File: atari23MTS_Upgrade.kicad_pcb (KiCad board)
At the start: 2 copper layers, 98 x 119.5 mm, 83 parts, among them J1 Conn_01x02, J2 Conn_01x02, J3 Conn_01x02, J4 Conn_01x02, J5 Conn_01x02, J6 Conn_01x02, J7 Conn_01x02, J8 Conn_01x02, J9 Micro_SD_Card_Det, P1 CONN_01X01, P2 CONN_01X01, P3 CONN_01X01, P4 CONN_01X01, P5 CONN_01X01, P6 CONN_01X01, P7 CONN_01X01, P8 CONN_01X01, SW1 SW_Push, U1 NCP1117ST33T3G, U10 74LVC2G32, U11 74LVC2G08, U12 74LVC2G74, U13 STM32F407VETx, U2 TXB0108-PW, U3 TXB0108-PW, U4 TXB0108-PW, U5 TXB0108-PW, U6 TXB0108-PW, U7 ISSI61WV5128BL, U8 ISSI61WV5128BL, U9 74HCT04

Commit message: Cosmetic issues
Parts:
- moved C1 7.62 mm to (123.2, 94.0)
- moved C11 7.62 mm to (121.2, 104.4)
- moved C2 7.62 mm to (103.6, 94.0)
- moved C3 7.62 mm to (104.9, 101.3)
- moved C6 7.62 mm to (139.7, 88.9)
- moved CART1 7.62 mm to (148.1, 133.9)
- moved CART2 7.62 mm to (166.4, 113.0)
- moved D1 7.62 mm to (113.5, 87.9)
- moved D2 7.62 mm to (113.5, 104.4)
- moved D4 7.62 mm to (147.3, 91.4)
- moved DUOCART 7.62 mm to (110.5, 76.2)
- moved ECI1 7.62 mm to (108.0, 147.3)
- moved ECI2 7.62 mm to (127.0, 113.0)
- moved EXTPWR1 7.62 mm to (108.0, 55.9)
- moved Kicad 7.62 mm to (155.0, 81.6)
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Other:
- board text added: "+12V"
- board text added: "+5V"
- board text added: "GND"

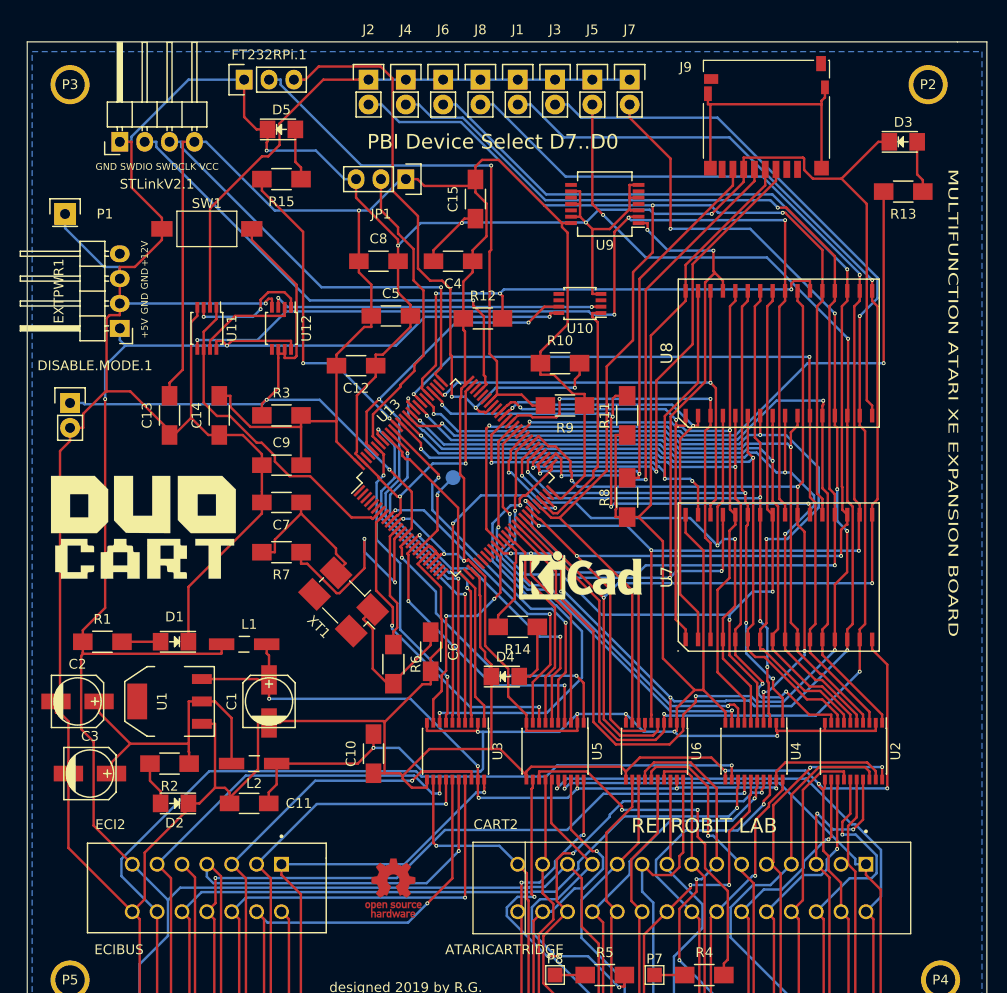
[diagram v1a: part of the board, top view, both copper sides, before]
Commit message: Modified CPU STM32F407VG
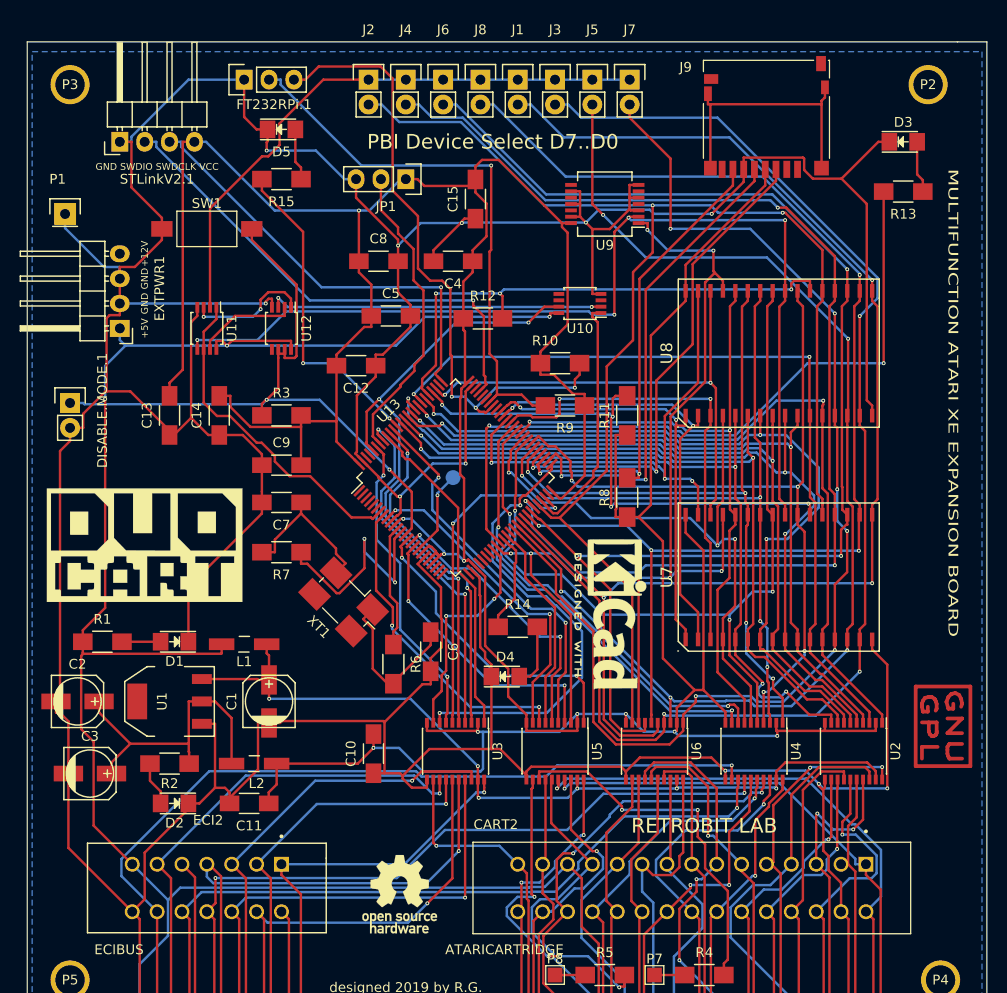
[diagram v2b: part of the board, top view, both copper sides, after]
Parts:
- removed ATARILOGO: LOGO, RetroBitLab:atari_fuji_SilkScreen_21.2x25-RevBack
- removed the DUOCART at (110.5, 76.2)
- removed Kicad: KiCad-Logo_5mm_SilkScreen, Symbol:KiCad-Logo_5mm_SilkScreen
- removed OSHW: OSHW-Logo_5.7x6mm_Copper, Symbol:OSHW-Logo_5.7x6mm_Copper
- added DUOCART: LOGO, RetroBitLab:DUOCart_20x11, F.Cu at (110.5, 78.0)
- added G***: LOGO, RetroBitLab:atari_fuji_SilkScreen_21.2x25-RevBack, B.Cu at (142.2, 55.9)
- added GPL: Symbol_GNU-GPL_CopperTop_Small, Symbol:Symbol_GNU-GPL_CopperTop_Small, F.Cu at (191.8, 96.5)
- added KICAD: KiCad-Logo2_6mm_SilkScreen, Symbol:KiCad-Logo2_6mm_SilkScreen, F.Cu at (158.8, 85.1)
- added REF**: OSHW-Logo_7.5x8mm_SilkScreen, Symbol:OSHW-Logo_7.5x8mm_SilkScreen, F.Cu at (136.5, 113.7)
- U13: value STM32F407VETx -> STM32F407VGTx
- moved G*** 2.84 mm to (142.2, 81.3)

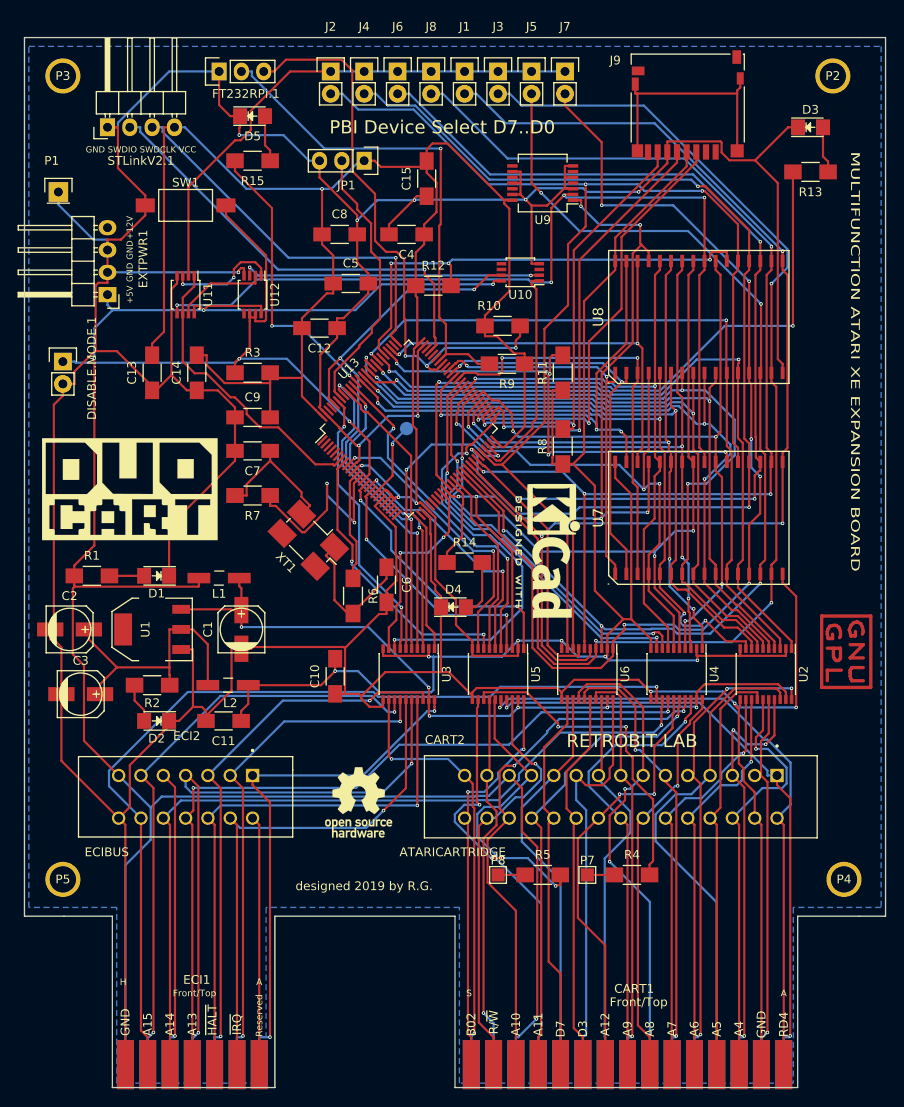
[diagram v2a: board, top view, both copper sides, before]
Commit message: added fill zone top layer
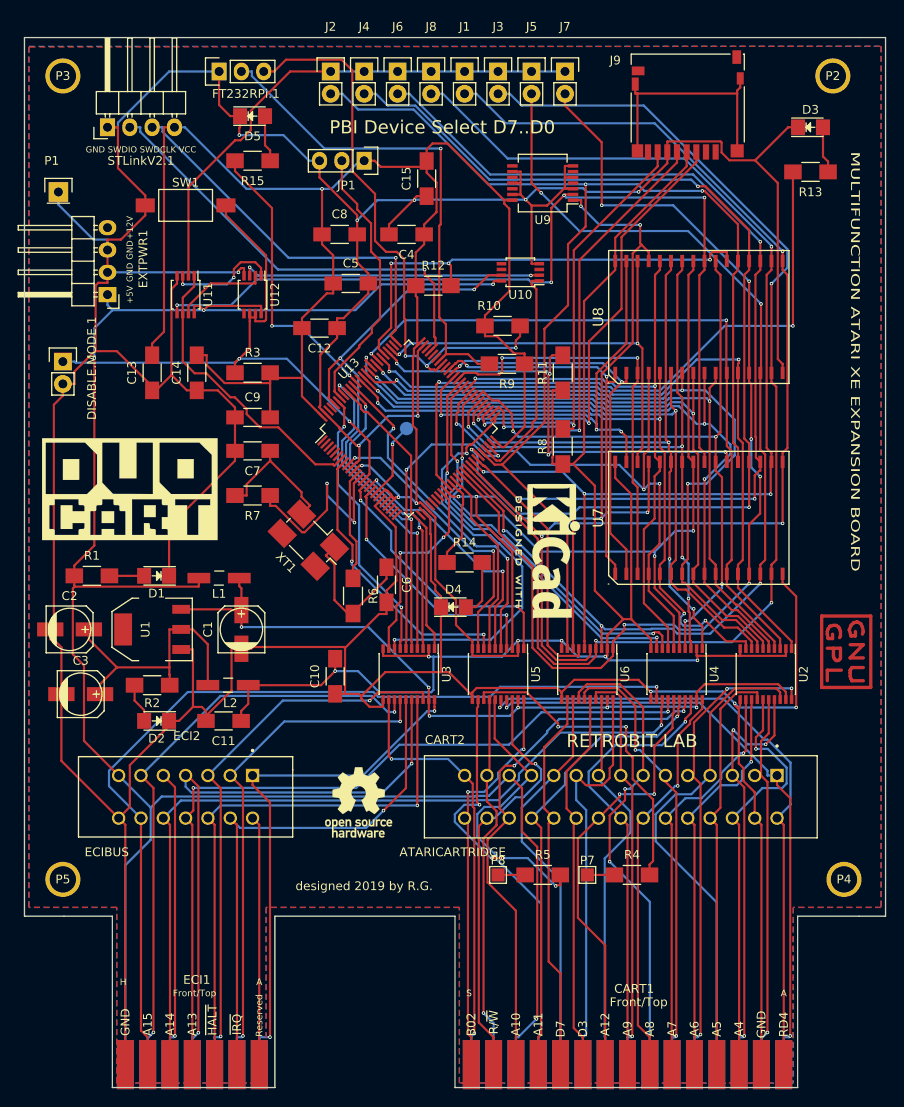
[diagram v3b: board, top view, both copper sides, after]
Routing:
- added copper zone on F.Cu, net GND
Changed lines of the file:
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@@
 (kicad_pcb (version 4) (host pcbnew 4.0.2+dfsg1-stable)
   (general
-    (links 0)
+    (links 357)
     (no_connects 0)
     (area 71.285716 17.15 198.15 162.820001)
@@
       )
     )
+  )
+  (zone (net 1) (net_name GND) (layer F.Cu) (hatch edge 0.508)
+    (connect_pads (clearance 0.508))
+    (min_thickness 0.254)
+    (fill yes (arc_segments 16) (thermal_gap 0.508) (thermal_bridge_width 0.508))
+    (polygon
+      (pts
+        (xy 99.1 27.7) (xy 196 27.6) (xy 196 125.6) (xy 186 125.6) (xy 185.9 145.6)
+        (xy 148 145.6) (xy 148 125.6) (xy 126 125.6) (xy 126 145.6) (xy 109 145.6)
+        (xy 109 125.6) (xy 99 125.6) (xy 99 27.7)
+      )
+    )

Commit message: Modified for dual processors board
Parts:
- removed DUOCART: LOGO, RetroBitLab:DUOCart_20x11
- removed G***: LOGO, RetroBitLab:atari_fuji_SilkScreen_21.2x25-RevBack
- removed G***: LOGO, RetroBitLab:atari_800_XL_BW_25x25
- removed GPL: Symbol_GNU-GPL_CopperTop_Small, Symbol:Symbol_GNU-GPL_CopperTop_Small
- removed J1, J2, J3, J4, J5, J6, J7, J8: Conn_01x02, Pin_Headers:Pin_Header_Straight_1x02
- removed KICAD: KiCad-Logo2_6mm_SilkScreen, Symbol:KiCad-Logo2_6mm_SilkScreen
- removed REF**: OSHW-Logo_7.5x8mm_SilkScreen, Symbol:OSHW-Logo_7.5x8mm_SilkScreen
- added C16: 20p, Capacitors_SMD:C_1206_HandSoldering, F.Cu at (390.3, 193.1)
- added C17: 20p, Capacitors_SMD:C_1206_HandSoldering, F.Cu at (385.0, 199.8)
- added C18: 100n, Capacitors_SMD:C_1206_HandSoldering, F.Cu at (405.9, 179.7)
- added C19: 100n, Capacitors_SMD:C_1206_HandSoldering, F.Cu at (397.4, 193.1)
- added C20: 100n, Capacitors_SMD:C_1206_HandSoldering, F.Cu at (383.3, 185.8)
- added C21: 100n, Capacitors_SMD:C_1206_HandSoldering, F.Cu at (392.1, 199.8)
- added C22: 100n, Capacitors_SMD:C_1206_HandSoldering, F.Cu at (404.4, 193.1)
- added C23: 100n, Capacitors_SMD:C_1206_HandSoldering, F.Cu at (411.5, 186.4)
- added C24: 100n, Capacitors_SMD:C_1206_HandSoldering, F.Cu at (399.1, 199.8)
- added DISABLE.MODE.2: CONN_01X02, Pin_Headers:Pin_Header_Straight_1x02, F.Cu at (348.2, 136.4)
- added JP2: CONN_01X03, Pin_Headers:Pin_Header_Straight_1x03, F.Cu at (336.8, 136.4)
- added P10: CONN_01X02, Pin_Headers:Pin_Header_Straight_1x02, F.Cu at (342.8, 193.2)
- added P11: CONN_01X02, Pin_Headers:Pin_Header_Straight_1x02, F.Cu at (329.8, 197.2)
- added P12: CONN_01X02, Pin_Headers:Pin_Header_Straight_1x02, F.Cu at (319.6, 207.9)
- added P13: CONN_01X02, Pin_Headers:Pin_Header_Straight_1x02, F.Cu at (353.0, 182.5)
- added P14: CONN_01X02, Pin_Headers:Pin_Header_Straight_1x02, F.Cu at (340.0, 204.0)
- added P9: CONN_01X02, Pin_Headers:Pin_Header_Straight_1x02, F.Cu at (319.6, 197.2)
- added R16: 220, Resistors_SMD:R_1206_HandSoldering, F.Cu at (391.8, 179.7)
- added STLinkV2.2: CONN_01X04, Pin_Headers:Pin_Header_Angled_1x04, F.Cu at (310.6, 136.4)
- added SW2: SW_Push, RetroBitLab:SW_SPST_FSMSM_3D, F.Cu at (341.0, 147.2)
- added U14: STM32F407VGTx, Housings_QFP:TQFP-100_14x14mm_Pitch0.5mm, F.Cu at (370.8, 186.8)
- added XT2: 8Mhz, RetroBitLab:Crystal_HC49-4H_Vertical_3D, F.Cu at (365.7, 201.9)
- D5: value LED.AMBER -> LED.GREEN
- P6: moved to F.Cu
- P7, P8: value CONN_01X01 -> CONN_01X02; footprint TestPoint:TestPoint_Pad_1.5x1.5mm -> Pin_Headers:Pin_Header_Straight_1x02
- R10: value 10k -> 0
- R11, R3: value 10K -> 220
- R13, R2: value 220 -> 10K
- R14, R15: value 220 -> 0
- R4: value 0 -> 10K
- R6: value 0 -> 220
- R7: value 220 -> 47k
- R8: value 47k -> 220
- R9: value 10k -> 220
- U13: footprint Housings_QFP:LQFP-100_14x14mm_Pitch0.5mm -> Housings_QFP:TQFP-100_14x14mm_Pitch0.5mm
- XT1: footprint Crystal:Crystal_SMD_0603-4Pin_6.0x3.5mm_HandSoldering -> RetroBitLab:Crystal_HC49-4H_Vertical_3D
- moved C5 353.1 mm to (479.8, 133.6)
- moved C4 350.0 mm to (479.8, 140.3), turned to 0 degrees
- moved U6 318.6 mm to (476.8, 151.3), turned to 0 degrees
- moved U5 318.3 mm to (466.4, 151.3), turned to 0 degrees
- moved R15 315.6 mm to (404.4, 186.4), turned to 0 degrees
- moved C13 310.5 mm to (414.2, 140.3), turned to 0 degrees
- moved U3 307.7 mm to (445.5, 151.3), turned to 0 degrees
- moved R7 303.1 mm to (421.2, 140.3), turned to 0 degrees
- moved U8 301.2 mm to (465.8, 138.0)
- moved C7 298.9 mm to (414.2, 147.0), turned to 0 degrees
- moved D5 296.7 mm to (384.0, 179.4)
- moved C11 294.5 mm to (414.2, 133.6)
- moved C15 291.5 mm to (421.2, 133.6), turned to 0 degrees
- moved C9 291.3 mm to (407.1, 140.3)
- moved C14 289.5 mm to (392.2, 157.8), turned to 0 degrees
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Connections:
- net BOOT0 renamed BOOT0_CART
- net SWDCLK renamed SWDCLK_CART
- net SWDIO renamed SWDIO_CART
- DISABLE.MODE.1 pad 1: nRESET -> nRESET_CART
- FT232RPi.1 pad 2: UART_RX_TTL -> UART_RX
- FT232RPi.1 pad 3: UART_TX_TTL -> UART_TX
- P7 pad 1: Net-(P7-Pad1) -> mD0
- P8 pad 1: Net-(P8-Pad1) -> mD1
- R10 pad 1: VCC3V3 -> Net-(R10-Pad1)
- R10 pad 2: UART_TX_TTL -> Net-(C16-Pad1)
- R11 pad 1: VCC3V3 -> Net-(R11-Pad1)
- R11 pad 2: ~mCHIP0 -> Net-(C17-Pad1)
- R12 pad 1: VCC3V3 -> GND
- R12 pad 2: ~mCHIP1 -> UART_TX
- R13 pad 1: Net-(D3-Pad2) -> GND
- R13 pad 2: LEDGRN -> UART_RX
- R14 pad 1: Net-(D4-Pad2) -> mB6
- R14 pad 2: LEDRED -> GND
- R15 pad 1: Net-(D5-Pad2) -> mB7
- R15 pad 2: LEDAMBER -> GND
- R2 pad 1: Net-(C2-Pad1) -> nRESET_CART
- R2 pad 2: Net-(D2-Pad2) -> VCC3V3
- R3 pad 1: nRESET -> Net-(C2-Pad1)
- R3 pad 2: VCC3V3 -> Net-(D2-Pad2)
- R4 pad 1: Net-(P7-Pad1) -> nRESET_MEM
- R4 pad 2: SPARE1 -> VCC3V3
- R5 pad 1: Net-(P8-Pad1) -> Net-(R5-Pad1)
- R5 pad 2: SPARE2 -> Net-(C6-Pad1)
- R6 pad 2: Net-(C6-Pad1) -> Net-(C7-Pad1)
- R7 pad 1: Net-(R7-Pad1) -> VCC3V3
- R7 pad 2: Net-(C7-Pad1) -> mSDO
- R8 pad 1: VCC3V3 -> Net-(D3-Pad2)
- R8 pad 2: mSDO -> LEDGRN
- R9 pad 1: VCC3V3 -> Net-(D4-Pad2)
- R9 pad 2: UART_RX_TTL -> LEDRED
- SW1 pad 2: nRESET -> nRESET_CART
- U12 pad 6: nRESET -> nRESET_MEM
- U12 pad 7: nRESET -> nRESET_MEM
- U13 pad 12: Net-(R6-Pad1) -> Net-(R5-Pad1)
- U13 pad 13: Net-(R7-Pad1) -> Net-(R6-Pad1)
- U13 pad 14: nRESET -> nRESET_CART
- U13 pad 18: TP1 -> (no net)
- U13 pad 47: ~mD8XX-DFXX -> (no net)
- U13 pad 48: ~mIRQ -> (no net)
- U13 pad 51: ~mREF -> (no net)
- U13 pad 63: mxA14 -> (no net)
- U13 pad 64: mxA15 -> (no net)
- U13 pad 65: mxA16 -> (no net)
- U13 pad 66: mxA17 -> (no net)
- U13 pad 68: UART_TX_TTL -> (no net)
- U13 pad 69: UART_RX_TTL -> (no net)
- U13 pad 7: mPBISEL -> (no net)
- U13 pad 78: mxA18 -> (no net)
- U13 pad 79: ~mCHIP0 -> (no net)
- U13 pad 8: mSPARE1 -> (no net)
- U13 pad 80: ~mCHIP1 -> (no net)
- U13 pad 89: LEDAMBER -> (no net)
- U13 pad 9: mSPARE2 -> (no net)
- U13 pad 91: ~mD1XX -> (no net)
- U13 pad 92: ~mEXSEL -> (no net)
- U13 pad 93: ~mHALT -> (no net)
- U13 pad 95: ~mRST -> (no net)
- U13 pad 96: ~mMPD -> (no net)
- U5 pad 12: SPARE2 -> (no net)
- U5 pad 13: SPARE1 -> (no net)
- U5 pad 8: mSPARE1 -> (no net)
- U5 pad 9: mSPARE2 -> (no net)
- U7 pad 1: mxA17 -> mB3
- U7 pad 2: mxA16 -> mB2
- U7 pad 22: ~mCHIP0 -> mB5
- U7 pad 3: mxA14 -> mB0
- U7 pad 30: mxA18 -> mB4
- U7 pad 31: mxA15 -> mB1
- U8 pad 1: mxA17 -> mB3
- U8 pad 2: mxA16 -> mB2
- U8 pad 22: ~mCHIP1 -> ~mB5
- U8 pad 3: mxA14 -> mB0
- U8 pad 30: mxA18 -> mB4
- U8 pad 31: mxA15 -> mB1
- U9 pad 3: GND -> mB5
- U9 pad 4: (no net) -> ~mB5
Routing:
- net GND: track 629.3 -> 0.00 mm, vias 11 -> 0
- net VCC3V3: track 429.5 -> 0.00 mm, vias 10 -> 0
- net +5VDC: track 243.0 -> 0.00 mm, vias 4 -> 0
- net mD7: track 142.6 -> 0.00 mm, vias 2 -> 0
- net mD2: track 136.9 -> 0.00 mm, vias 3 -> 0
- net mD6: track 134.9 -> 0.00 mm, vias 4 -> 0
- net mD5: track 134.8 -> 0.00 mm, vias 3 -> 0
- net mD3: track 134.2 -> 0.00 mm, vias 3 -> 0
- net mD4: track 127.9 -> 0.00 mm, vias 4 -> 0
- net mD0: track 124.7 -> 0.00 mm, vias 6 -> 0
- net mD1: track 122.5 -> 0.00 mm, vias 5 -> 0
- net A15: track 103.5 -> 0.00 mm, vias 1 -> 0
- net mW/~R: track 103.1 -> 0.00 mm, vias 4 -> 0
- net mR/~W: track 96.3 -> 0.00 mm, vias 6 -> 0
- net A14: track 92.8 -> 0.00 mm, vias 1 -> 0
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- removed copper zone on B.Cu, net GND
- removed copper zone on F.Cu, net GND
